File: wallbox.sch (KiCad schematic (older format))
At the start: 28 parts, among them J1 From Transformer, J2 To Wallbox, J3 To Microcontroller, Q1 BC547, Q2 BC547, Q3 BC547, U1 KA78R33, U2 LM7805, U3 TPC817MC, U4 TPC817MC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

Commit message: Footprint associations and imports
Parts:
- removed RL1, RL2, RL3: HE101, symbol FINDER-32.21-x300
- added RL1, RL2, RL3: HE721A0510, wallbox-footprints:HE700 DIL, symbol HE721A0510
- C2: footprint (none) -> Capacitors_THT:CP_Radial_D10.0mm_P5.00mm
- D1, D2: footprint (none) -> wallbox-footprints:D-BRIDGE-WOG
- J1: footprint (none) -> Connectors_Terminal_Blocks:TerminalBlock_Pheonix_PT-3.5mm_3pol
- J2, J3: footprint (none) -> Connectors_Terminal_Blocks:TerminalBlock_Pheonix_PT-3.5mm_6pol
- R1, R2, R4, R5, R6, R7, R8, R9: footprint (none) -> Resistors_THT:R_Axial_DIN0204_L3.6mm_D1.6mm_P5.08mm_Horizontal
- U2: footprint (none) -> TO_SOT_Packages_THT:TO-220_Vertical
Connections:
- wire segments 96 -> 97
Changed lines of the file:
@@
 EESchema Schematic File Version 2
+LIBS:wallbox-rescue
 LIBS:power
 LIBS:device
@@
 LIBS:relays
 LIBS:diode
+LIBS:wallbox-components
 LIBS:wallbox-cache
 EELAYER 25 0
@@
 F 0 "J1" H 1500 1650 50  0000 C TNN
 F 1 "From Transformer" V 1350 1300 50  0000 C TNN
-F 2 "" H 1500 975 50  0001 C CNN
+F 2 "Connectors_Terminal_Blocks:TerminalBlock_Pheonix_PT-3.5mm_3pol" H 1500 975 50  0001 C CNN
 F 3 "" H 1475 1400 50  0001 C CNN
 	1    1500 1300
@@
 F 0 "J2" H 7150 2250 50  0000 C TNN
 F 1 "To Wallbox" V 7000 1600 50  0000 C TNN
-F 2 "" H 7150 975 50  0001 C CNN
+F 2 "Connectors_Terminal_Blocks:TerminalBlock_Pheonix_PT-3.5mm_6pol" H 7150 975 50  0001 C CNN
 F 3 "" H 7125 2000 50  0001 C CNN
 	1    7150 1600
@@
 25¢
 $Comp
-L FINDER-32.21-x300 RL1
-U 1 1 59CEDD07
-P 6350 2850
-F 0 "RL1" H 6800 3000 50  0000 L CNN
-F 1 "HE101" H 6800 2900 50  0000 L CNN
-F 2 "" H 6350 2850 50  0001 C CNN
-F 3 "" H 6350 2850 50  0001 C CNN
-	1    6350 2850
-	1    0    0    -1
-$EndComp
-$Comp
-L FINDER-32.21-x300 RL2
-U 1 1 59CEDDF0
-P 6350 3700
-F 0 "RL2" H 6800 3850 50  0000 L CNN
-F 1 "HE101" H 6800 3750 50  0000 L CNN
-F 2 "" H 6350 3700 50  0001 C CNN
-F 3 "" H 6350 3700 50  0001 C CNN
-	1    6350 3700
-	1    0    0    -1
-$EndComp
-$Comp
-L FINDER-32.21-x300 RL3
-U 1 1 59CEDE89
-P 6350 4600
-F 0 "RL3" H 6800 4750 50  0000 L CNN
-F 1 "HE101" H 6800 4650 50  0000 L CNN
-F 2 "" H 6350 4600 50  0001 C CNN
-F 3 "" H 6350 4600 50  0001 C CNN
-	1    6350 4600
-	1    0    0    -1
-$EndComp
-$Comp
 L D_Bridge_+A-A D1
 U 1 1 59CEE417
@@
 F 0 "D1" H 2250 2475 50  0000 L CNN
 F 1 "2W005G" H 2250 2400 50  0000 L CNN
-F 2 "" H 2200 2200 50  0001 C CNN
+F 2 "wallbox-footprints:D-BRIDGE-WOG" H 2200 2200 50  0001 C CNN
 F 3 "" H 2200 2200 50  0001 C CNN
 	1    2200 2200
@@
 F 0 "R1" V 2830 3300 50  0000 C CNN
 F 1 "2.2k" V 2750 3300 50  0000 C CNN
-F 2 "" V 2680 3300 50  0001 C CNN
+F 2 "Resistors_THT:R_Axial_DIN0204_L3.6mm_D1.6mm_P5.08mm_Horizontal" V 2680 3300 50  0001 C CNN
 F 3 "" H 2750 3300 50  0001 C CNN
 	1    2750 3300
@@
 F 0 "R2" V 3130 3100 50  0000 C CNN
 F 1 "1k" V 3050 3100 50  0000 C CNN
-F 2 "" V 2980 3100 50  0001 C CNN
+F 2 "Resistors_THT:R_Axial_DIN0204_L3.6mm_D1.6mm_P5.08mm_Horizontal" V 2980 3100 50  0001 C CNN
 F 3 "" H 3050 3100 50  0001 C CNN
 	1    3050 3100
@@
 F 0 "J3" H 3500 5450 50  0000 C TNN
 F 1 "To Microcontroller" V 3350 4800 50  0000 C TNN
-F 2 "" H 3500 4175 50  0001 C CNN
+F 2 "Connectors_Terminal_Blocks:TerminalBlock_Pheonix_PT-3.5mm_6pol" H 3500 4175 50  0001 C CNN
 F 3 "" H 3475 5200 50  0001 C CNN
 	1    3500 4800
@@
 F 0 "D2" H 3550 2475 50  0000 L CNN
 F 1 "2W005G" H 3550 2400 50  0000 L CNN
-F 2 "" H 3500 2200 50  0001 C CNN
+F 2 "wallbox-footprints:D-BRIDGE-WOG" H 3500 2200 50  0001 C CNN
 F 3 "" H 3500 2200 50  0001 C CNN
 	1    3500 2200
@@
 F 0 "C2" H 5225 2150 50  0000 L CNN
 F 1 "10uF" H 5225 1950 50  0000 L CNN
-F 2 "" H 5238 1900 50  0001 C CNN
+F 2 "Capacitors_THT:CP_Radial_D10.0mm_P5.00mm" H 5238 1900 50  0001 C CNN
 F 3 "" H 5200 2050 50  0001 C CNN
 	1    5200 2050
@@
 F 0 "R4" V 5180 2850 50  0000 C CNN
 F 1 "1k" V 5100 2850 50  0000 C CNN
-F 2 "" V 5030 2850 50  0001 C CNN
+F 2 "Resistors_THT:R_Axial_DIN0204_L3.6mm_D1.6mm_P5.08mm_Horizontal" V 5030 2850 50  0001 C CNN
 F 3 "" H 5100 2850 50  0001 C CNN
 	1    5100 2850
@@
 F 0 "R5" V 5180 3700 50  0000 C CNN
 F 1 "1k" V 5100 3700 50  0000 C CNN
-F 2 "" V 5030 3700 50  0001 C CNN
+F 2 "Resistors_THT:R_Axial_DIN0204_L3.6mm_D1.6mm_P5.08mm_Horizontal" V 5030 3700 50  0001 C CNN
 F 3 "" H 5100 3700 50  0001 C CNN
 	1    5100 3700
@@
 F 0 "R6" V 5180 4600 50  0000 C CNN
 F 1 "1k" V 5100 4600 50  0000 C CNN
-F 2 "" V 5030 4600 50  0001 C CNN
+F 2 "Resistors_THT:R_Axial_DIN0204_L3.6mm_D1.6mm_P5.08mm_Horizontal" V 5030 4600 50  0001 C CNN
 F 3 "" H 5100 4600 50  0001 C CNN
 	1    5100 4600
@@
 	6950 1700 6650 1700
 Wire Wire Line
-	6650 1700 6650 2550
-Wire Wire Line
 	6950 1900 6800 1900
 Wire Wire Line
 	6800 1900 6800 3400
 Wire Wire Line
-	6800 3400 6650 3400
-Wire Wire Line
-	6950 2100 6950 4300
-Wire Wire Line
-	6950 4300 6650 4300
+	6800 3400 6550 3400
+Wire Wire Line
+	6950 4300 6950 2100
+Wire Wire Line
+	6550 4300 6950 4300
 Wire Wire Line
 	7100 4900 6550 4900
@@
 	6550 4000 7100 4000
 Connection ~ 7100 4000
-Wire Wire Line
-	6550 3150 7100 3150
-Connection ~ 7100 3150
 Wire Wire Line
 	2200 1900 2200 1100
@@
 F 0 "R7" V 3680 4350 50  0000 C CNN
 F 1 "1k" V 3600 4350 50  0000 C CNN
-F 2 "" V 3530 4350 50  0001 C CNN
+F 2 "Resistors_THT:R_Axial_DIN0204_L3.6mm_D1.6mm_P5.08mm_Horizontal" V 3530 4350 50  0001 C CNN
 F 3 "" H 3600 4350 50  0001 C CNN
 	1    3600 4350
@@
 F 0 "R8" V 3880 4350 50  0000 C CNN
 F 1 "1k" V 3800 4350 50  0000 C CNN
-F 2 "" V 3730 4350 50  0001 C CNN
+F 2 "Resistors_THT:R_Axial_DIN0204_L3.6mm_D1.6mm_P5.08mm_Horizontal" V 3730 4350 50  0001 C CNN
 F 3 "" H 3800 4350 50  0001 C CNN
 	1    3800 4350
@@
 F 0 "R9" V 4080 4350 50  0000 C CNN
 F 1 "1k" V 4000 4350 50  0000 C CNN
-F 2 "" V 3930 4350 50  0001 C CNN
+F 2 "Resistors_THT:R_Axial_DIN0204_L3.6mm_D1.6mm_P5.08mm_Horizontal" V 3930 4350 50  0001 C CNN
 F 3 "" H 4000 4350 50  0001 C CNN
 	1    4000 4350
@@
 F 0 "U2" H 4850 1604 50  0000 C CNN
 F 1 "LM7805" H 4700 2000 50  0000 C CNN
-F 2 "" H 4700 1800 50  0001 C CNN
+F 2 "TO_SOT_Packages_THT:TO-220_Vertical" H 4700 1800 50  0001 C CNN
 F 3 "" H 4700 1800 50  0001 C CNN
 	1    4700 1800
@@
 Wire Wire Line
 	3900 1750 4300 1750
+$Comp
+L HE721A0510 RL1
+U 1 1 59D04393
+P 6350 2850
+F 0 "RL1" H 6800 3000 50  0000 L CNN
+F 1 "HE721A0510" H 6800 2900 50  0000 L CNN
+F 2 "wallbox-footprints:HE700 DIL" H 6350 2850 50  0001 C CNN
+F 3 "" H 6350 2850 50  0001 C CNN
+	1    6350 2850
+	1    0    0    -1
+$EndComp
+Wire Wire Line
+	6550 3150 7100 3150
+Connection ~ 7100 3150
+Connection ~ 6650 3150
+Wire Wire Line
+	6650 1700 6650 2550
+Wire Wire Line
+	6650 2550 6550 2550
+$Comp
+L HE721A0510 RL2
+U 1 1 59D05106
+P 6350 3700
+F 0 "RL2" H 6800 3850 50  0000 L CNN
+F 1 "HE721A0510" H 6800 3750 50  0000 L CNN
+F 2 "wallbox-footprints:HE700 DIL" H 6350 3700 50  0001 C CNN
+F 3 "" H 6350 3700 50  0001 C CNN
+	1    6350 3700
+	1    0    0    -1
+$EndComp
+$Comp
+L HE721A0510 RL3
+U 1 1 59D0516B
+P 6350 4600
+F 0 "RL3" H 6800 4750 50  0000 L CNN
+F 1 "HE721A0510" H 6800 4650 50  0000 L CNN
+F 2 "wallbox-footprints:HE700 DIL" H 6350 4600 50  0001 C CNN
+F 3 "" H 6350 4600 50  0001 C CNN
+	1    6350 4600
+	1    0    0    -1
+$EndComp
+Connection ~ 6650 3400
+Connection ~ 6650 4300
+Connection ~ 6650 4000
+Connection ~ 6650 4900
 $EndSCHEMATC

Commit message: Final footprint association fixups
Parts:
- C1: footprint (none) -> Capacitors_THT:CP_Radial_D10.0mm_P5.00mm
- R3: footprint (none) -> Resistors_THT:R_Axial_DIN0204_L3.6mm_D1.6mm_P5.08mm_Horizontal
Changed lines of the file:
@@
 EESchema Schematic File Version 2
-LIBS:wallbox-rescue
 LIBS:power
 LIBS:device
@@
 F 0 "C1" H 2225 2800 50  0000 L CNN
 F 1 "0.22uF" H 2225 2600 50  0000 L CNN
-F 2 "" H 2238 2550 50  0001 C CNN
+F 2 "Capacitors_THT:CP_Radial_D10.0mm_P5.00mm" H 2238 2550 50  0001 C CNN
 F 3 "" H 2200 2700 50  0001 C CNN
 	1    2200 2700
@@
 F 0 "R3" V 4180 2850 50  0000 C CNN
 F 1 "1k" V 4100 2850 50  0000 C CNN
-F 2 "" V 4030 2850 50  0001 C CNN
+F 2 "Resistors_THT:R_Axial_DIN0204_L3.6mm_D1.6mm_P5.08mm_Horizontal" V 4030 2850 50  0001 C CNN
 F 3 "" H 4100 2850 50  0001 C CNN
 	1    4100 2850

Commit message: Footprint change
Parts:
- RL1, RL2, RL3: footprint wallbox-footprints:HE700 DIL -> wallbox-footprints:HE700_DIP-14
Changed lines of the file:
@@
 F 0 "RL1" H 6800 3000 50  0000 L CNN
 F 1 "HE721A0510" H 6800 2900 50  0000 L CNN
-F 2 "wallbox-footprints:HE700 DIL" H 6350 2850 50  0001 C CNN
+F 2 "wallbox-footprints:HE700_DIP-14" H 6350 2850 50  0001 C CNN
 F 3 "" H 6350 2850 50  0001 C CNN
 	1    6350 2850
@@
 F 0 "RL2" H 6800 3850 50  0000 L CNN
 F 1 "HE721A0510" H 6800 3750 50  0000 L CNN
-F 2 "wallbox-footprints:HE700 DIL" H 6350 3700 50  0001 C CNN
+F 2 "wallbox-footprints:HE700_DIP-14" H 6350 3700 50  0001 C CNN
 F 3 "" H 6350 3700 50  0001 C CNN
 	1    6350 3700
@@
 F 0 "RL3" H 6800 4750 50  0000 L CNN
 F 1 "HE721A0510" H 6800 4650 50  0000 L CNN
-F 2 "wallbox-footprints:HE700 DIL" H 6350 4600 50  0001 C CNN
+F 2 "wallbox-footprints:HE700_DIP-14" H 6350 4600 50  0001 C CNN
 F 3 "" H 6350 4600 50  0001 C CNN
 	1    6350 4600

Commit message: Component fixups and initial PCB layout
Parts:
- removed U2: LM7805, TO_SOT_Packages_THT:TO-220_Vertical, symbol LM7805
- added U2: LM7805CT, TO_SOT_Packages_THT:TO-220_Vertical, symbol LM7805CT
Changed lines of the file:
@@
 	3200 4200 4500 4200
 Connection ~ 3200 4200
-$Comp
-L LM7805 U2
-U 1 1 59CF8CCB
-P 4700 1800
-F 0 "U2" H 4850 1604 50  0000 C CNN
-F 1 "LM7805" H 4700 2000 50  0000 C CNN
-F 2 "TO_SOT_Packages_THT:TO-220_Vertical" H 4700 1800 50  0001 C CNN
-F 3 "" H 4700 1800 50  0001 C CNN
-	1    4700 1800
-	1    0    0    -1
-$EndComp
 Text Notes 3600 4600 1    60   ~ 0
 5¢
@@
 Connection ~ 6650 4000
 Connection ~ 6650 4900
+$Comp
+L LM7805CT U2
+U 1 1 59D2B7B1
+P 4700 1800
+F 0 "U2" H 4500 2000 50  0000 C CNN
+F 1 "LM7805CT" H 4700 2000 50  0000 L CNN
+F 2 "TO_SOT_Packages_THT:TO-220_Vertical" H 4700 1900 50  0001 C CIN
+F 3 "" H 4700 1800 50  0001 C CNN
+	1    4700 1800
+	1    0    0    -1
+$EndComp
 $EndSCHEMATC

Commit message: Schematic checkpointing
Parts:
- removed C1: 0.22uF, Capacitors_THT:CP_Radial_D10.0mm_P5.00mm, symbol C
- removed J1: From Transformer, Connectors_Terminal_Blocks:TerminalBlock_Pheonix_PT-3.5mm_3pol, symbol Screw_Terminal_1x03
- removed R1: 2.2k, Resistors_THT:R_Axial_DIN0204_L3.6mm_D1.6mm_P5.08mm_Horizontal, symbol R
- added C1: 2.2uF, Capacitors_THT:CP_Radial_D10.0mm_P2.50mm, symbol CP
- added C3, C4: 0.1uF, Capacitors_THT:C_Disc_D5.0mm_W2.5mm_P5.00mm, symbol C
- added C5: 2000uF, symbol CP
- added C6: 0.33uF, symbol C
- added C7: 0.1uF, symbol C
- added D3: 1N4007, symbol D
- added J1: From Transformer, symbol Screw_Terminal_1x04
- added R10: 10k, Resistors_THT:R_Axial_DIN0204_L3.6mm_D1.6mm_P5.08mm_Horizontal, symbol R
- added U7: 74HC14, Housings_DIP:DIP-14_W7.62mm, symbol 74HC14
- R3: value 1k -> 47k
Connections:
- wire segments 97 -> 140
- no-connect marks 2 -> 7
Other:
- note added: "Center"
- moved on the sheet: C2, J3, R3, U2

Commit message: Cloned more components into local library
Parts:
- D1, D2: symbol D_Bridge_+A-A -> 2W005G
- J1: symbol Screw_Terminal_1x04 -> Screw_Terminal_Transformer
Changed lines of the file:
@@
 LIBS:diode
 LIBS:wallbox-components
+LIBS:dc-dc
 LIBS:wallbox-cache
 EELAYER 25 0
@@
 25¢
 $Comp
-L D_Bridge_+A-A D1
+L 2W005G D1
 U 1 1 59CEE417
 P 2200 2200
@@
 Signal
 $Comp
-L D_Bridge_+A-A D2
+L 2W005G D2
 U 1 1 59CF2604
 P 3500 2200
@@
 	6950 1900 6800 1900
 Wire Wire Line
-	6800 3400 6800 1900
-Wire Wire Line
-	6550 3400 6800 3400
+	6800 1900 6800 3400
+Wire Wire Line
+	6800 3400 6550 3400
 Wire Wire Line
 	6950 4300 6950 2100
@@
 Connection ~ 5900 4550
 $Comp
-L Screw_Terminal_1x04 J1
+L Screw_Terminal_Transformer J1
 U 1 1 59D94102
 P 1500 1400

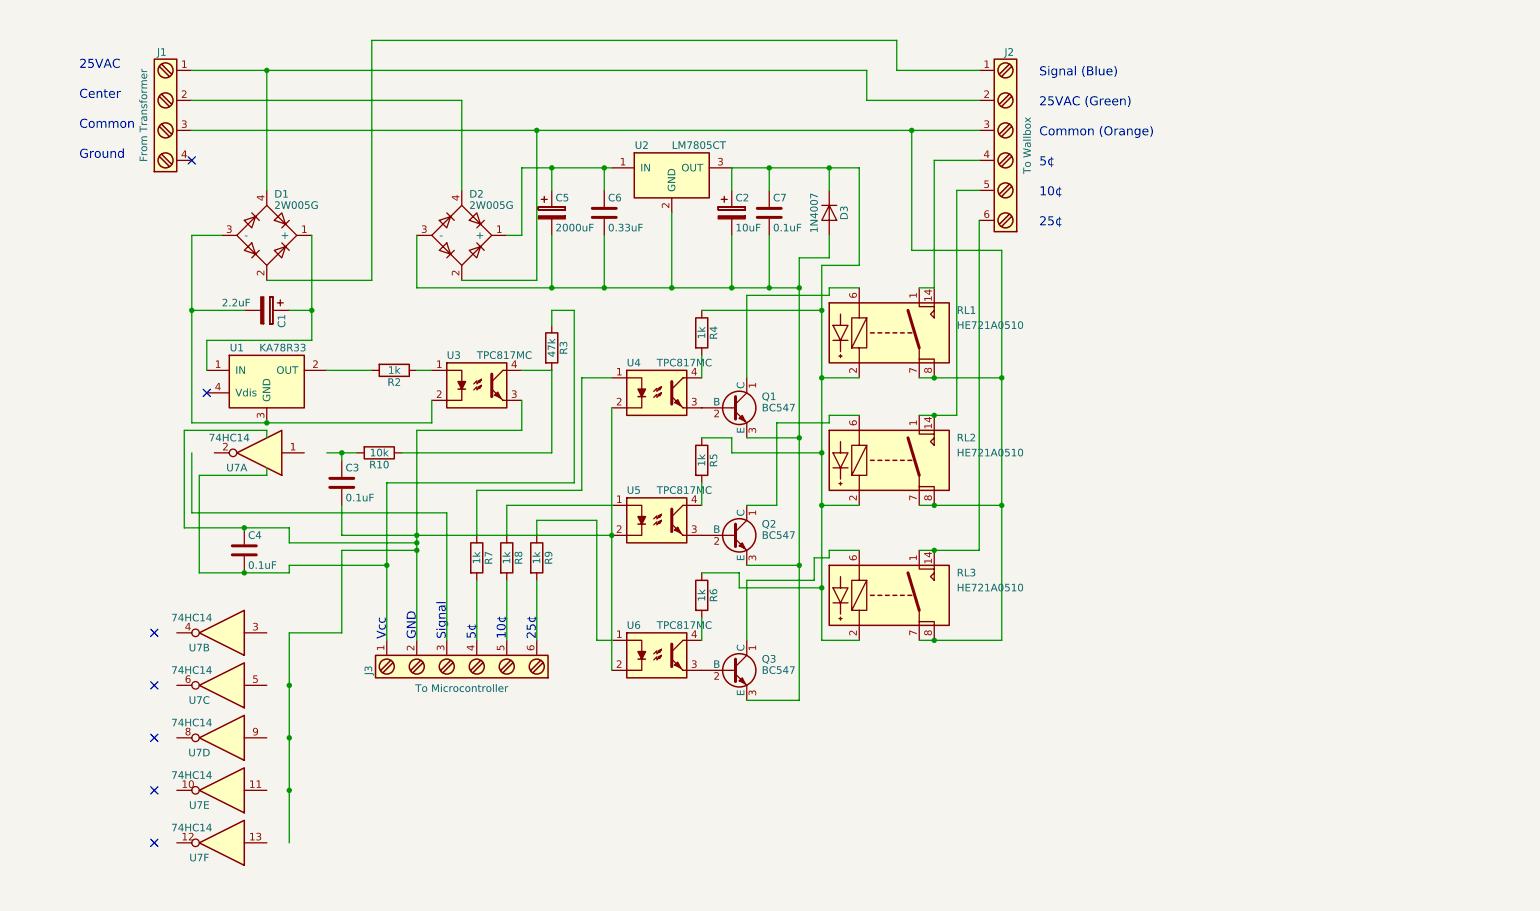
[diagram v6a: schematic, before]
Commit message: Schematic redraw
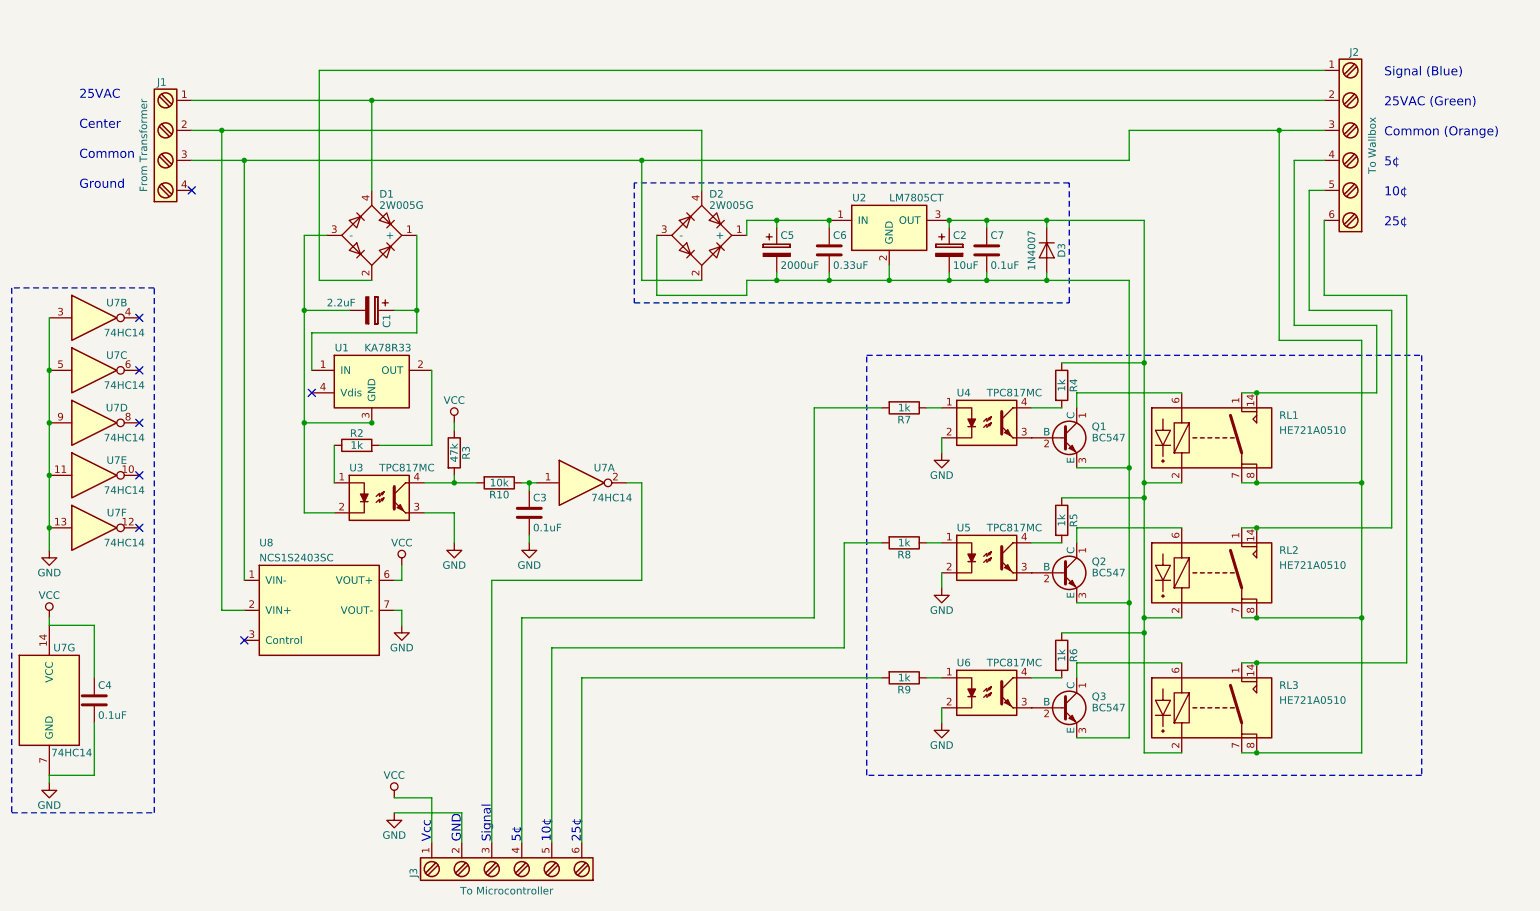
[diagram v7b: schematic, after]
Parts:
- added unit 7 of U7
- added U8: NCS1S2403SC, symbol NCS1S2403SC
- U7: footprint Housings_DIP:DIP-14_W7.62mm -> (none)
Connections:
- net labels added: GND, VCC
- wire segments 140 -> 128
- no-connect marks 7 -> 8
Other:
- moved on the sheet: C1, C2, C3, C4, C5, C6, C7, D1, D2, D3, J1, J2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
